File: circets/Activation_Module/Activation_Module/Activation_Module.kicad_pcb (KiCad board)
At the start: 2 copper layers, 101.9 x 199.4 mm, 50 parts, among them J1 Bus_Connector, J2 Conn_01x03_Male, SW1 SW_DIP_x04, SW2 SW_DIP_x04, U1 74HC541, U10 74HC541, U11 74HC541, U12 74LS86, U13 74LS86, U14 74HC541, U15 74LS32, U16 74LS32, U17 74HC541, U18 74HC00, U19 74LS08, U2 AM-Connector, U20 74157, U21 74157, U22 74LS32, U3 74HC541, U4 74LS86, U5 74LS86, U6 74LS32, U7 74LS32, U8 74HC541, U9 74HC541

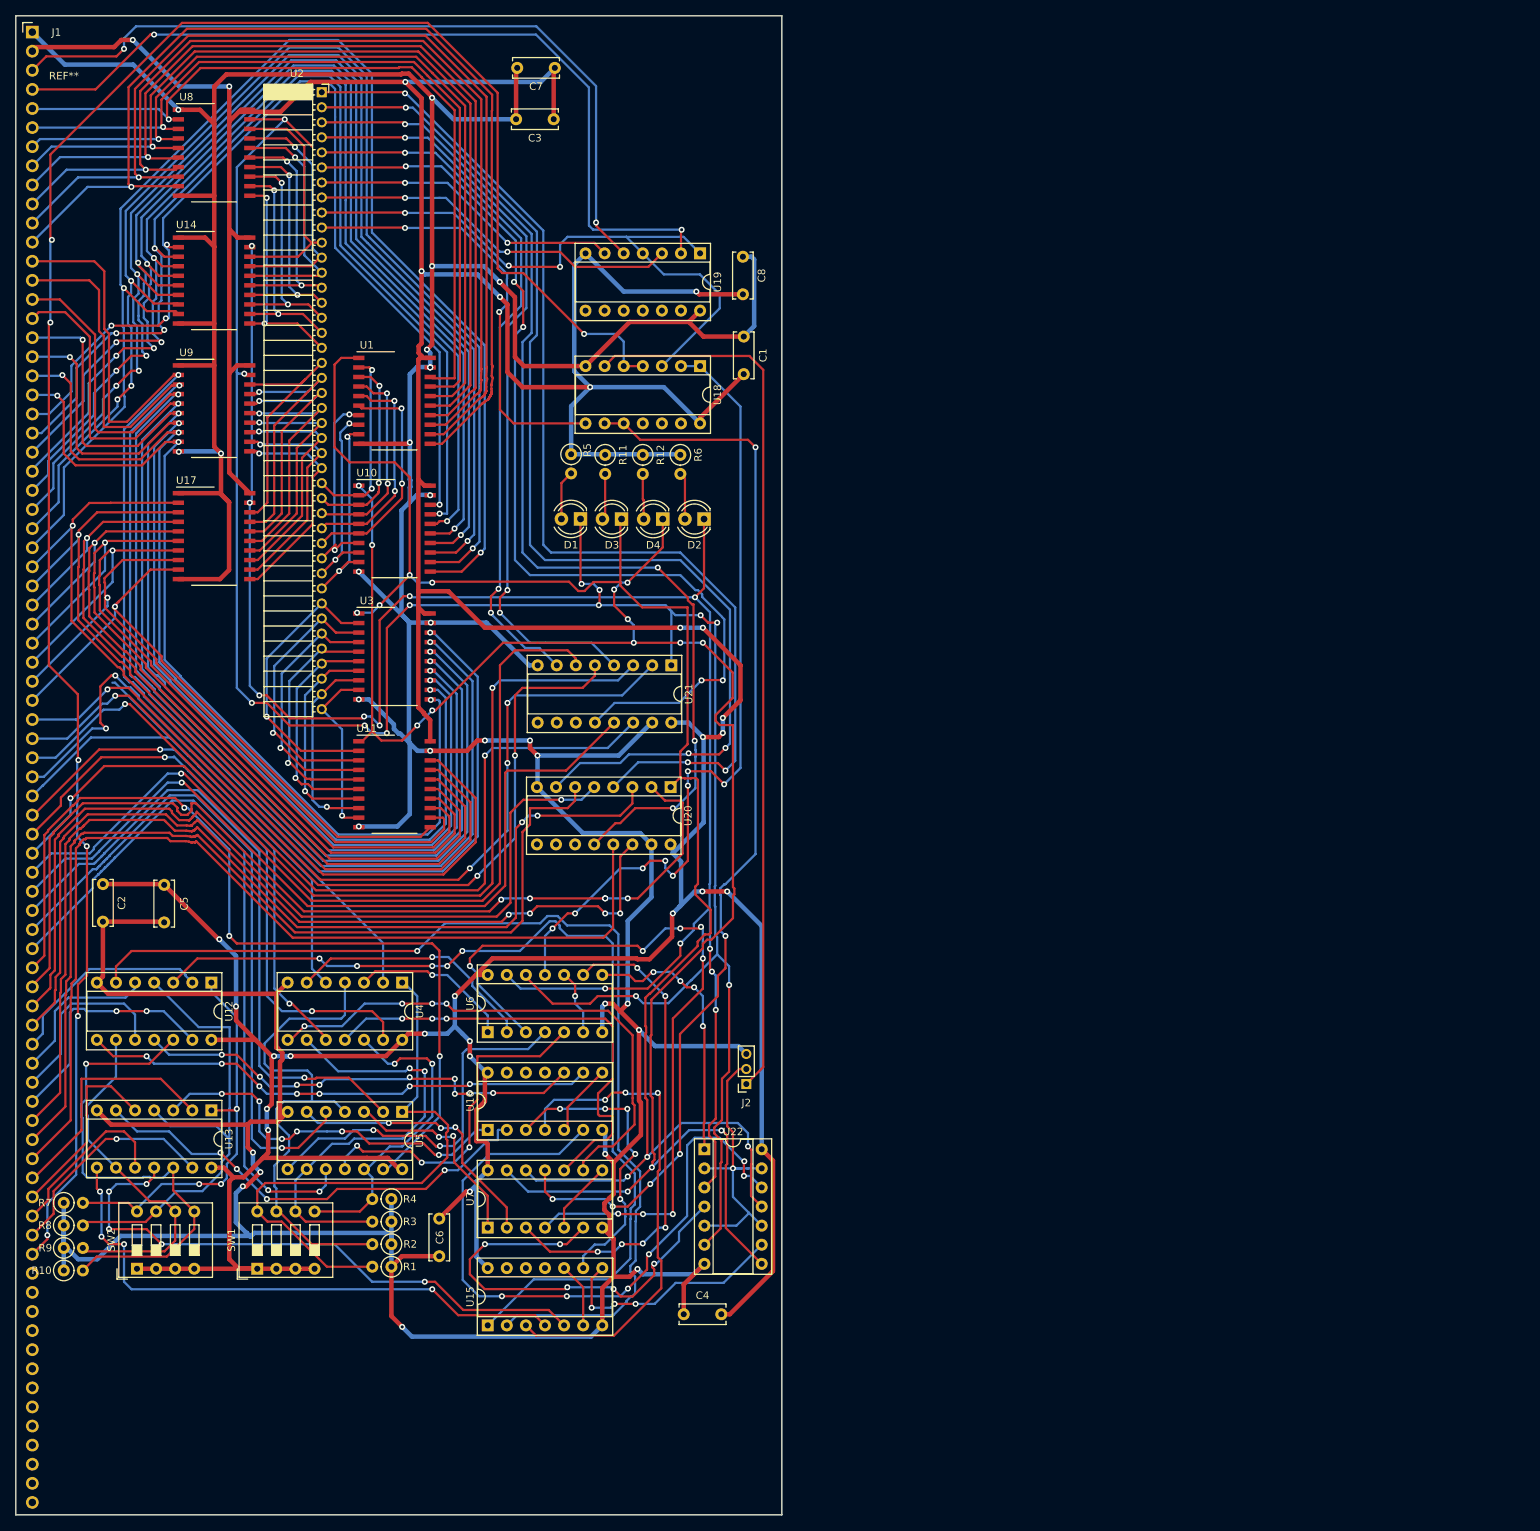
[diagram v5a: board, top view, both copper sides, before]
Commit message: Added Name and other notest to AM PCB-Layout
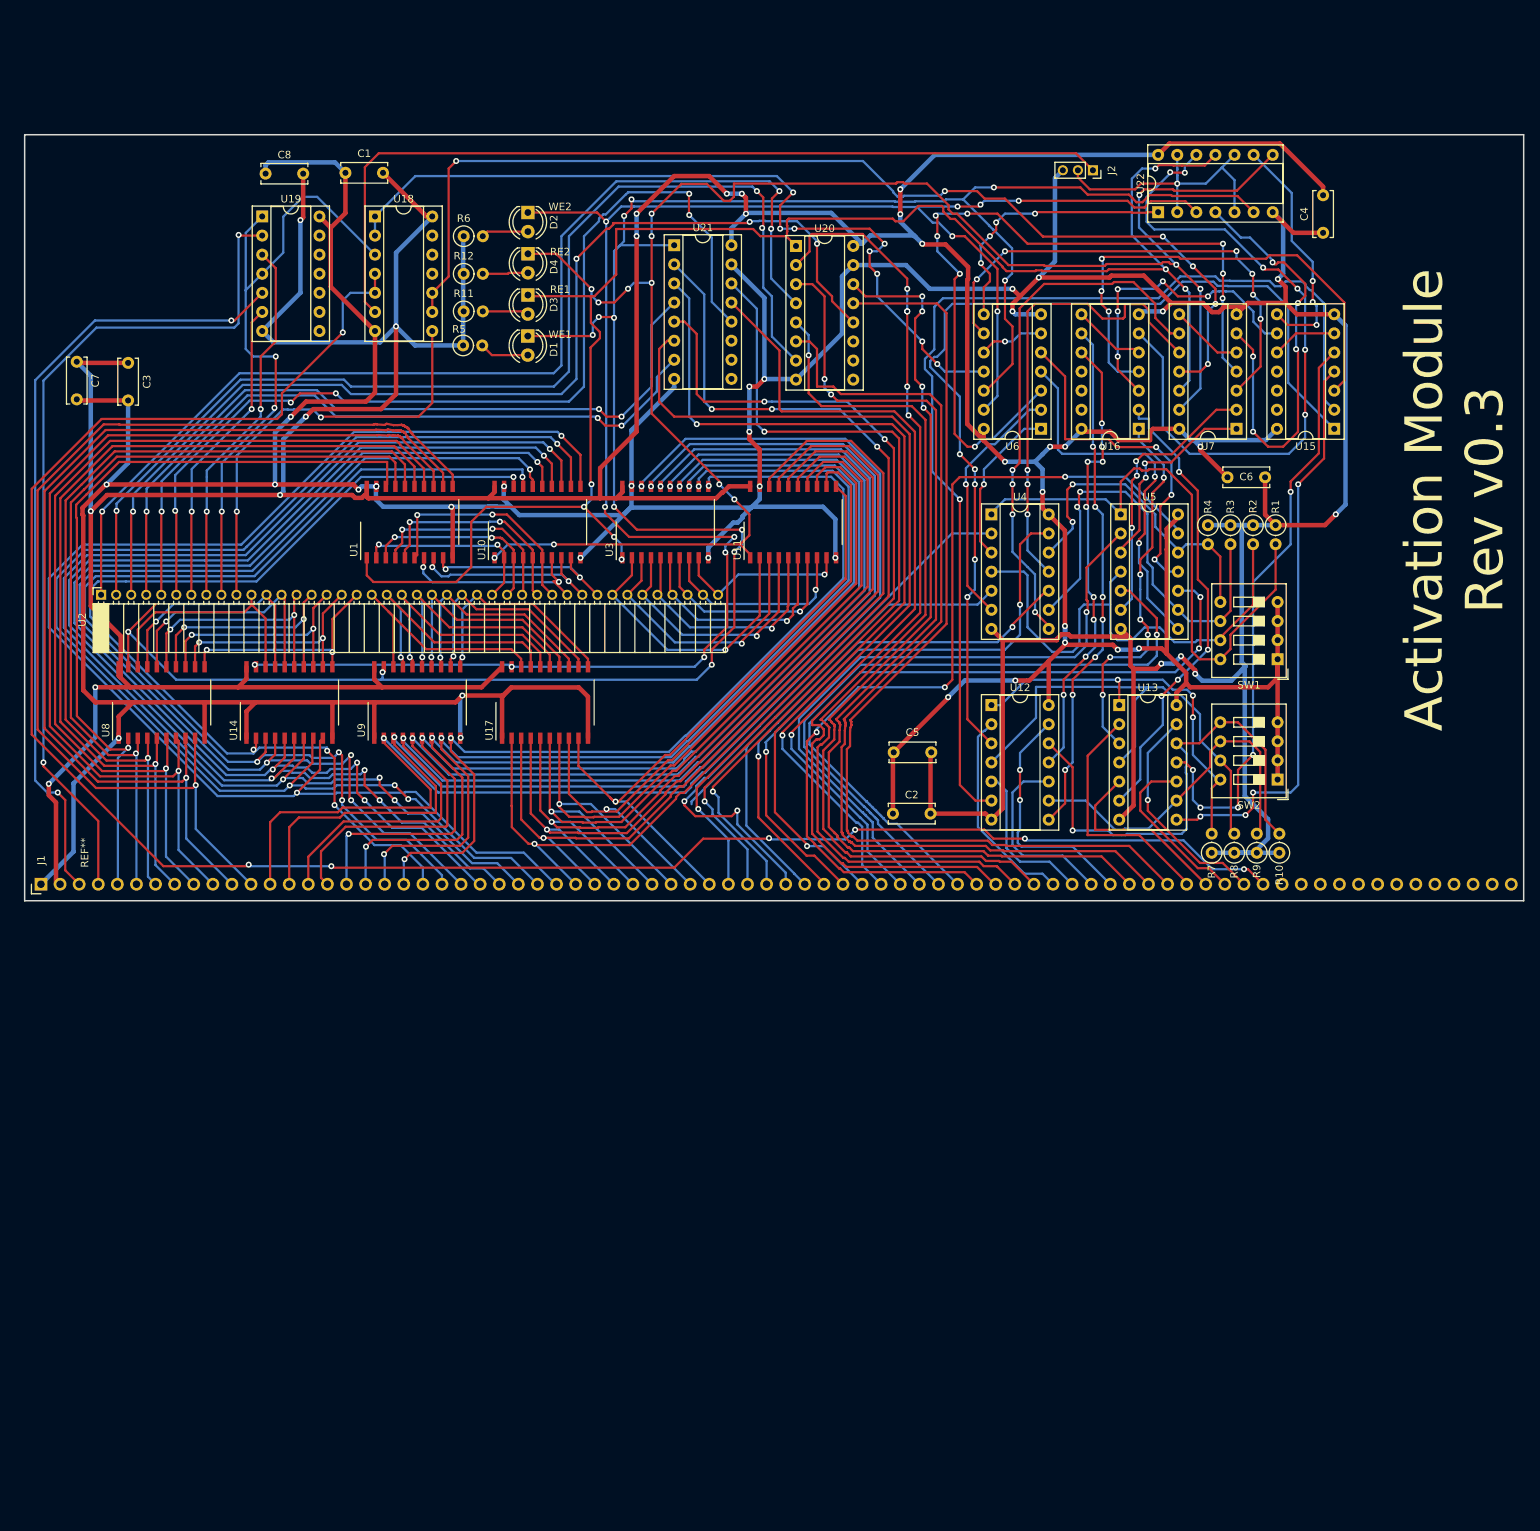
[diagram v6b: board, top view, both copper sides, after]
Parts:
- moved R10 171.0 mm to (195.7, 124.9), turned to 90 degrees
- moved R9 167.2 mm to (192.7, 124.9), turned to 90 degrees
- moved C4 167.1 mm to (201.5, 42.5), turned to 90 degrees
- moved SW2 165.1 mm to (195.4, 115.2), turned to 180 degrees
- moved U15 164.0 mm to (203.0, 68.5), turned to 180 degrees
- moved R8 163.4 mm to (189.7, 124.9), turned to 90 degrees
- moved R7 159.6 mm to (186.7, 124.9), turned to 90 degrees
- moved SW1 158.1 mm to (195.4, 99.2), turned to 180 degrees
- moved R1 153.5 mm to (195.2, 81.4), turned to -90 degrees
- moved C6 151.0 mm to (193.8, 75.0), turned to 180 degrees
- moved R2 149.3 mm to (192.2, 81.4), turned to -90 degrees
- moved U7 145.6 mm to (190.0, 68.5), turned to 180 degrees
- moved R3 145.1 mm to (189.2, 81.4), turned to -90 degrees
- moved R4 140.8 mm to (186.2, 81.4), turned to -90 degrees
- moved U22 138.5 mm to (179.6, 39.7), turned to 90 degrees
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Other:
- board size 101.9 x 199.4 mm -> 199.4 x 101.9 mm
- board text added: "Activation Module Rev v0.3"
- board text added: "RE1"
- board text added: "RE2"
- board text added: "WE1"
- board text added: "WE2"
